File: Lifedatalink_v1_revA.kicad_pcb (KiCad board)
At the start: 4 copper layers, 76.6 x 59.8 mm, 90 parts, among them J1 DX07S024XJ1R1100, J10 503480-0400, J11 5034801400, J12 5034801400, J13 503480-0600, J14 503480-0600, J15 503480-0600, J16 503480-0600, J17 503480-0600, J18 ECG_RIGHT_LEG, J2 BATTERY CONNECTOR, J3 503480-0600, J4 Conn_01x06, J5 503480-0600, J6 ECG_LEFT_ARM, J7 ECG_RIGHT_ARM, J8 503480-0600, J9 503480-0400, P6 HORIZON MEDICAL LOGO, Q1 DMG2301L, SW1 SW_Push, U1 BL654, U2 LP5907MFX-3_3_NOPB, U3 ADS1292R, U4 MCP73831-2-OT, U5 TMP117NAIYBGR, U6 MAX30102, U7 LP5907MFX-1.8, U8 IIS2DLPCTR, U9 PCA9306, Y1 Crystal

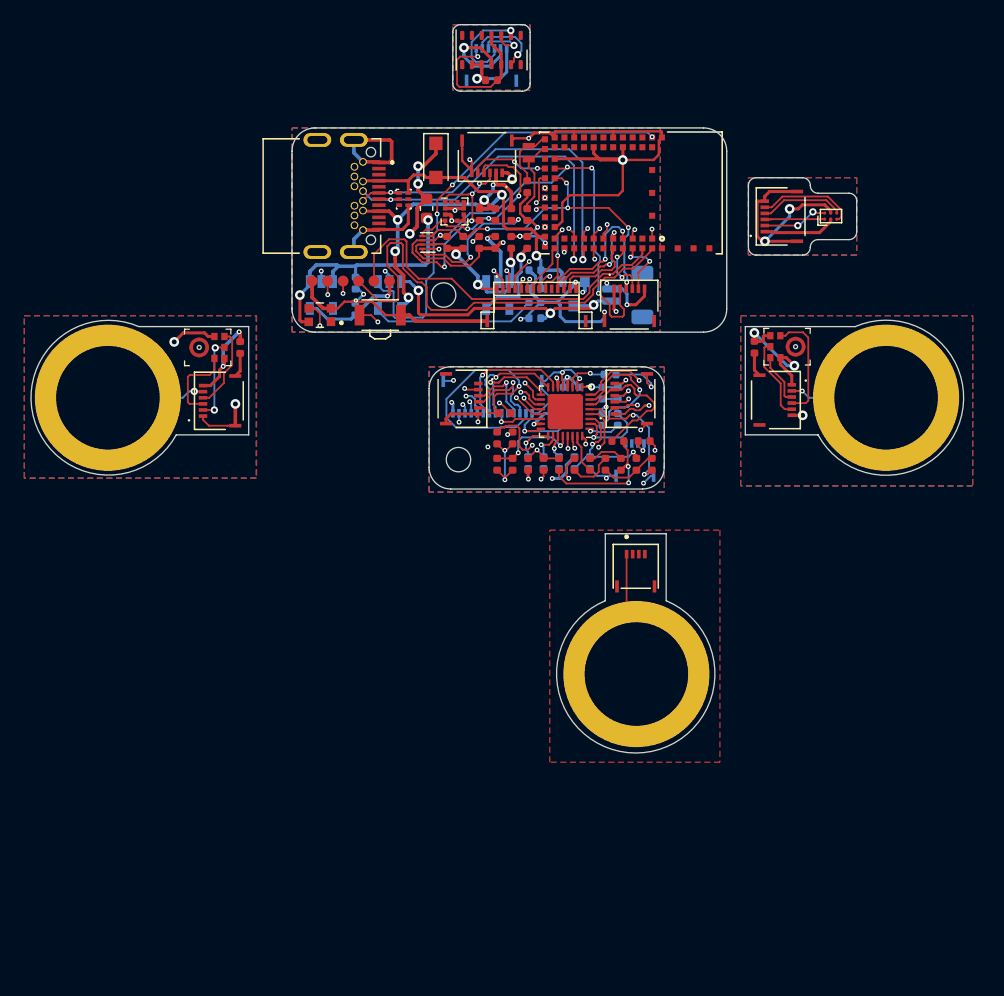
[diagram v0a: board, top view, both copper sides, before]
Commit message: Fix temperature sensor thermal pad, mounting holes, silk screen, mic ground, capacitor symmetric location and routing
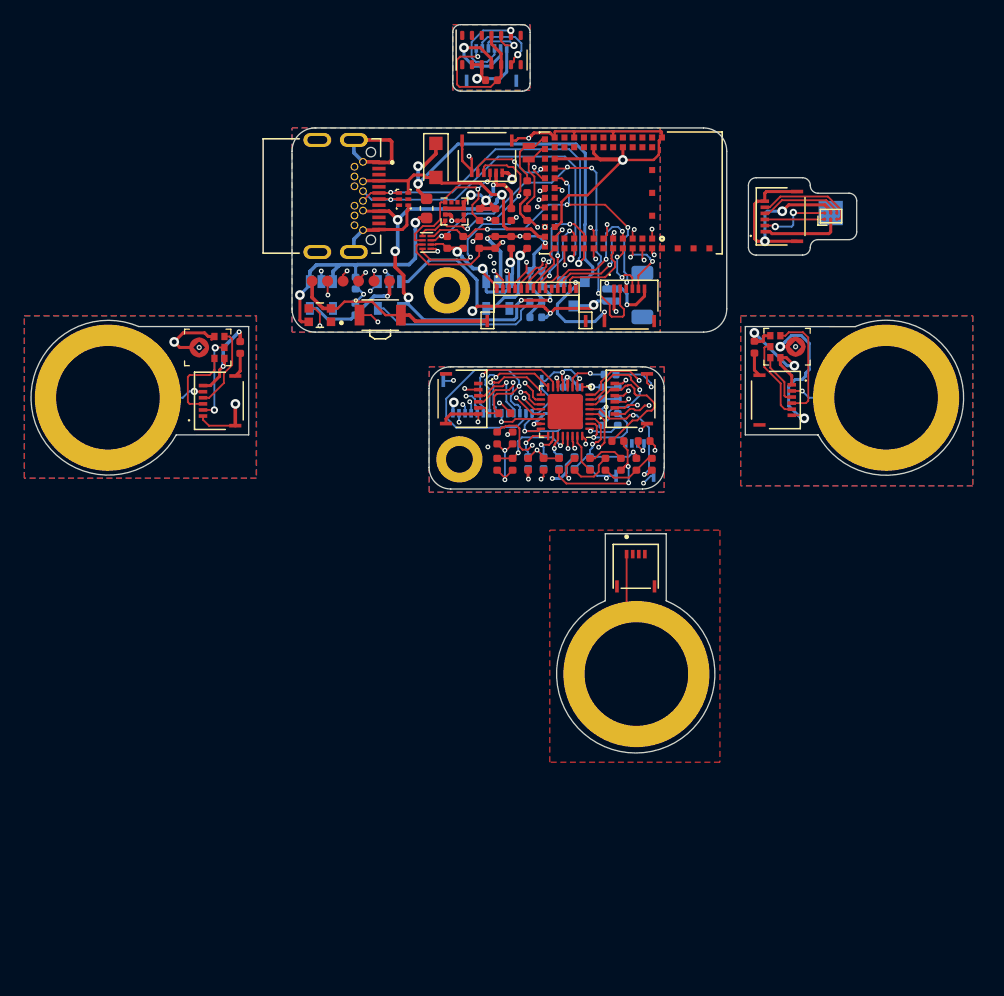
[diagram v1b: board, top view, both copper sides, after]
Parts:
- removed REF** (x2): MountingHole_2mm, MountingHole:MountingHole_2mm
- added J19: MOUNTING_HOLE_MAIN, MountingHole:MountingHole_2.2mm_M2_DIN965_Pad, F.Cu at (81.6, 107.8)
- added J20: MOUNTING_HOLE_ECG, MountingHole:MountingHole_2.2mm_M2_DIN965_Pad, F.Cu at (80.6, 93.9)
- added TPAD: TEMP_SENSOR_PAD, Pads_1.27mm:TEMP_SENSOR_PAD, B.Cu at (112.1, 87.6)
- P6: footprint horizon_logo_silk:horizon_logo_silk -> horizon_logo_silk:horizon_logo_silk_small
- moved P6 12.4 mm to (98.8, 86.7)
- moved R4 0.18 mm to (87.9, 93.6)
- moved C7 0.11 mm to (87.9, 96.1)
- moved C6 0.09 mm to (87.9, 92.3)
- moved R3 0.08 mm to (87.9, 94.9)
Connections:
- U1 pad 34: Net-(U1-Pad34) -> /MCP73831_STAT
- U1 pad 63: /MCP73831_STAT -> Net-(U1-Pad63)
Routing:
- net GND: track 242.4 -> 294.3 mm, vias 38 -> 37
- net /MCP73831_STAT: track 36.5 -> 21.9 mm, vias 3 -> 2
- net +5V: track 47.7 -> 59.0 mm, vias 5 -> 6
- net /BL654_UART_TX: track 27.5 -> 21.5 mm
- net /BL654_UART_RX: track 28.5 -> 23.0 mm
- net +3V3: track 130.8 -> 136.1 mm
- net /BL654_SWDIO: track 37.3 -> 32.3 mm, vias 0 -> 3
- net /VIN_FUSE: track 27.4 -> 32.3 mm, vias 4 -> 2
- net /BL654_I2C_SCL_LV: track 17.9 -> 13.8 mm, vias 4 -> 2
- net +BATT: track 23.0 -> 25.2 mm
- net /ADS_SPI_MOSI: track 11.8 -> 10.0 mm
- net /BL654_SWDCLK: track 30.3 -> 31.6 mm, vias 0 -> 3
- net /~ADS_SPI_CS: track 5.87 -> 7.14 mm
- net /~ADS_PWDN_RESET: track 10.5 -> 9.44 mm
- net +1V8: track 45.6 -> 44.6 mm
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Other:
- board text added: "Designed by HORIZON MEDICAL S.A.S. Cartagena - Colombia www.horizonmedical.co Model: LDL1A"
- board text removed: "LifeDataLinkv1RevA"

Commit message: Finished post routing schematic pinout and footprint cross check
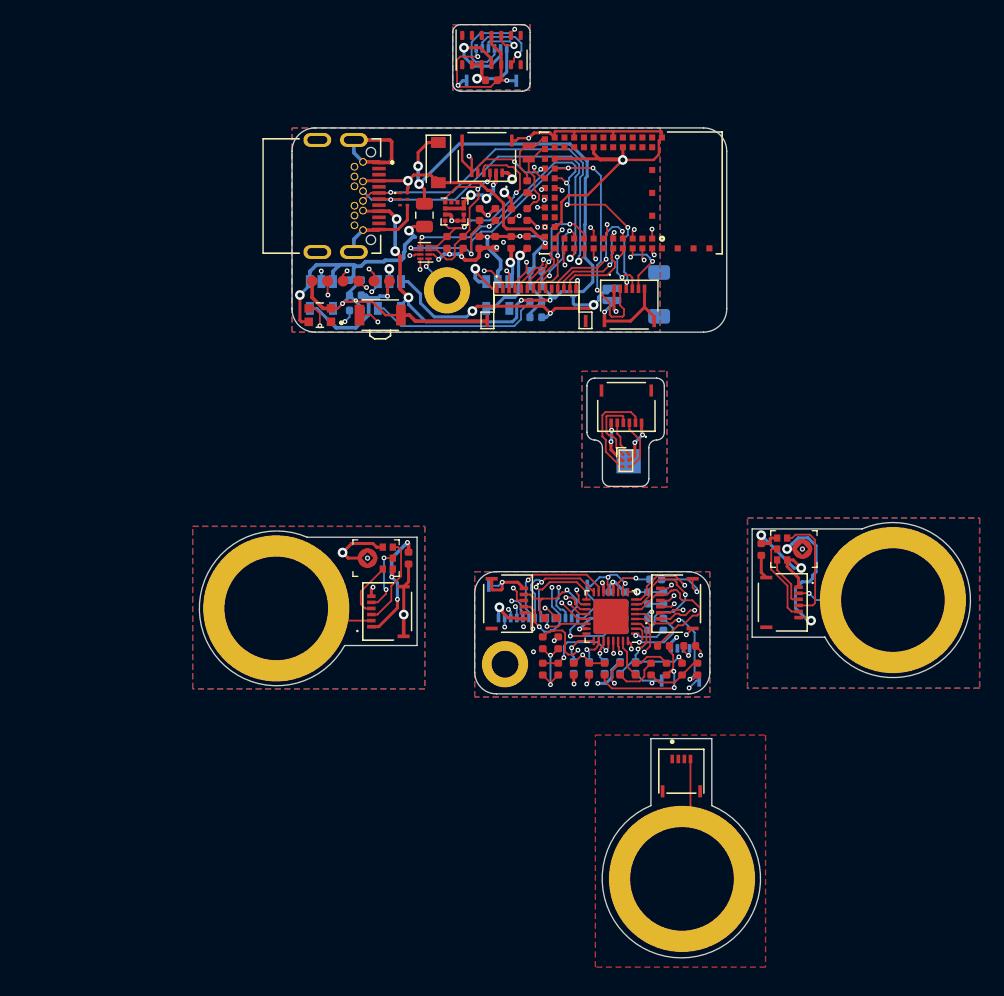
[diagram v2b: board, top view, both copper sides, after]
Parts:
- removed BAT: 401030, Battery:401030
- removed TPAD: TEMP_SENSOR_PAD, Pads_1.27mm:TEMP_SENSOR_PAD
- added C31: 100pF, Capacitor_SMD:C_0402_1005Metric, B.Cu at (73.1, 95.6)
- added REF**: TEMP_SENSOR_PAD, Pads_1.27mm:TEMP_SENSOR_PAD, B.Cu at (95.5, 108.0)
- D1: footprint digikey-footprints:UFDFN-6_1.45x1mm -> SnapEda:SON50P100X145X60-6N
- D3: footprint Diode_SMD:D_SOD-123F -> Diode_SMD:D_SOD-123
- F1: value 0603L075SLYR -> 0ZCK0075FF2E; footprint Fuse:Fuse_0603_1608Metric -> Fuse:Fuse_0805_2012Metric
- J2: value BATTERY CONNECTOR -> SM02B-SRSS-TB(LF)(SN); footprint Connector_JST:JST_SH_BM02B-SRSS-TB_1x02-1MP_P1.00mm_Vertical -> Connector_JST:JST_SH_SM02B-SRSS-TB_1x02-1MP_P1.00mm_Horizontal
- Q1: value DMG2301L -> CSD23280F3; footprint Package_TO_SOT_SMD:SOT-23 -> SnapEda:TRANS_CSD23280F3
- moved U5 26.2 mm to (95.3, 107.9), turned to 0 degrees
- moved J17 22.1 mm to (75.8, 120.3)
- moved J7 22.1 mm to (66.6, 120.0)
- moved C29 22.1 mm to (77.4, 115.9)
- moved MIC1 22.1 mm to (74.1, 115.9)
- moved J13 20.1 mm to (95.3, 103.4), turned to 180 degrees
- moved C10 17.2 mm to (98.4, 119.2)
- moved C11 17.2 mm to (97.7, 117.7)
- moved C12 17.2 mm to (93.5, 124.9)
- moved C13 17.2 mm to (98.4, 121.3)
- moved C14 17.2 mm to (97.1, 121.3)
- moved C15 17.2 mm to (93.5, 125.0)
- moved C16 17.2 mm to (98.6, 125.0)
- moved C18 17.2 mm to (97.3, 125.0)
- moved C20 17.2 mm to (99.9, 125.0)
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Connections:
- J10 pad 1: /ECG_RIGHT_LEG -> GND
- J10 pad 4: Net-(J10-Pad4) -> /ECG_RIGHT_LEG
- J13 pad 1: +3V3 -> GND
- J13 pad 2: /BL654_I2C_SCL_HV_EXT -> /TMP_ADD0_EXT
- J13 pad 3: /BL654_I2C_SDA_HV_EXT -> /TMP_ALERT_EXT
- J13 pad 4: /TMP_ALERT_EXT -> /BL654_I2C_SDA_HV_EXT
- J13 pad 5: /TMP_ADD0_EXT -> /BL654_I2C_SCL_HV_EXT
- J13 pad 6: GND -> +3V3
- J17 pad 1: GND -> +3V3
- J17 pad 2: /BL654_I2S_SD_EXT -> /ECG_RIGHT_ARM
- J17 pad 3: /BL654_I2S_SCK_EXT -> /BL654_I2S_WS_EXT
- J17 pad 4: /BL654_I2S_WS_EXT -> /BL654_I2S_SCK_EXT
- J17 pad 5: /ECG_RIGHT_ARM -> /BL654_I2S_SD_EXT
- J17 pad 6: +3V3 -> GND
- J8 pad 1: Net-(J8-Pad1) -> GND
- J8 pad 2: /ECG_RIGHT_ARM -> /BL654_I2S_SD_EXT
- J8 pad 3: /BL654_I2S_WS_EXT -> /BL654_I2S_SCK_EXT
- J8 pad 4: /BL654_I2S_SCK_EXT -> /BL654_I2S_WS_EXT
- J8 pad 5: /BL654_I2S_SD_EXT -> /ECG_RIGHT_ARM
- J8 pad 6: GND -> +3V3
- J9 pad 4: Net-(J9-Pad4) -> GND
- R17 pad 1: +1V8 -> +3V3
- R18 pad 1: +3V3 -> +1V8
- R18 pad 2: /BL654_I2C_SDA_HV -> /BL654_I2C_SDA_LV
- R19 pad 1: +3V3 -> +1V8
- R19 pad 2: /BL654_I2C_SCL_HV -> /BL654_I2C_SCL_LV
- R20 pad 1: +1V8 -> +3V3
- R20 pad 2: /BL654_I2C_SCL_LV -> /BL654_I2C_SCL_HV
- R21 pad 1: +1V8 -> +3V3
- R21 pad 2: /BL654_I2C_SDA_LV -> /BL654_I2C_SDA_HV
- U9 pad 2: +3V3 -> +1V8
- U9 pad 3: /BL654_I2C_SCL_HV -> /BL654_I2C_SCL_LV
- U9 pad 4: /BL654_I2C_SDA_HV -> /BL654_I2C_SDA_LV
- U9 pad 5: /BL654_I2C_SDA_LV -> /BL654_I2C_SDA_HV
- U9 pad 6: /BL654_I2C_SCL_LV -> /BL654_I2C_SCL_HV
- U9 pad 7: +1V8 -> +3V3
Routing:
- net GND: track 294.3 -> 275.5 mm, vias 37 -> 39
- net /BL654_I2S_SD_EXT: track 49.5 -> 33.5 mm
- net Net-(C31-Pad2): track 11.4 -> 21.1 mm, vias 2 -> 3
- net /BL654_I2C_SCL_HV: track 33.8 -> 40.3 mm, vias 4 -> 5
- net /BL654_I2C_SDA_HV: track 26.8 -> 32.8 mm, vias 5 -> 6
- net +1V8: track 44.6 -> 39.5 mm, vias 6 -> 9
- net +3V3: track 136.1 -> 140.8 mm, vias 21 -> 26
- net +5V: track 59.0 -> 54.3 mm
- net /BL654_I2C_SCL_HV_EXT: track 6.06 -> 2.99 mm, vias 2 -> 0
- net /BL654_I2S_WS_EXT: track 29.2 -> 32.1 mm, vias 2 -> 3
- net /TMP_ALERT_EXT: track 6.91 -> 4.44 mm
- net /VIN_FUSE: track 32.3 -> 34.3 mm
- net /ADS_SPI_SCLK: track 16.7 -> 18.3 mm
- net /ECG_RIGHT_ARM: track 34.6 -> 33.1 mm, vias 4 -> 3
- net +BATT: track 25.2 -> 23.8 mm
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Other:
- board size 76.6 x 59.8 mm -> 63.3 x 76.6 mm

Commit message: Added battery level voltage divider
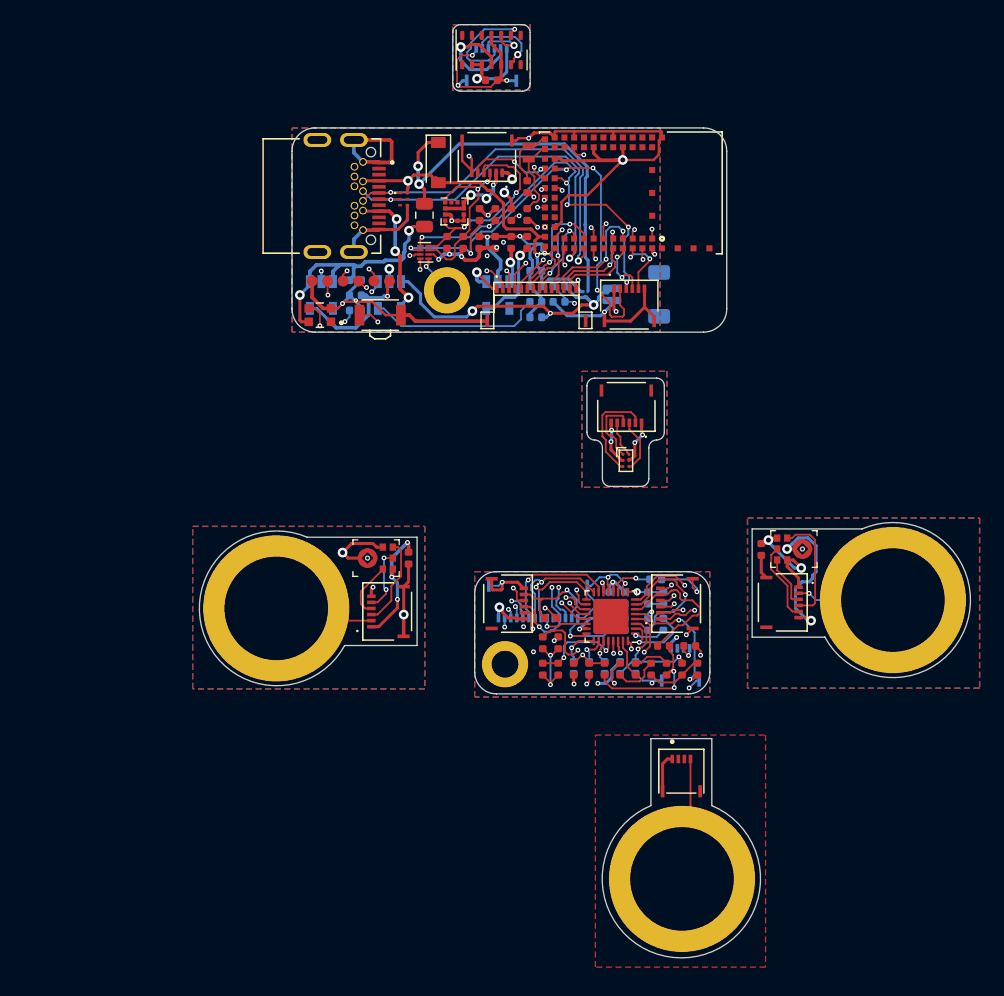
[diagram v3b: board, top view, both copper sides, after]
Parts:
- removed REF**: TEMP_SENSOR_PAD, Pads_1.27mm:TEMP_SENSOR_PAD
- added R1: 100K, Resistor_SMD:R_0402_1005Metric, B.Cu at (89.8, 93.6)
- added R2: 100K, Resistor_SMD:R_0402_1005Metric, B.Cu at (89.8, 94.9)
- moved Q1 0.99 mm to (91.9, 94.2)
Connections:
- U1 pad 48: Net-(U1-Pad48) -> /VDIV
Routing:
- net /VDIV: track 0.00 -> 20.2 mm, vias 0 -> 2
- net GND: track 275.5 -> 294.0 mm
- net +5V: track 54.3 -> 44.0 mm, vias 6 -> 5
- net +3V3: track 140.8 -> 138.6 mm
- net +BATT: track 23.8 -> 25.5 mm
- net /VIN_FUSE: track 34.3 -> 32.9 mm
- net +1V8: track 39.5 -> 40.8 mm
- net /VIN: track 20.6 -> 20.1 mm

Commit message: Changed the color of FFC connectors
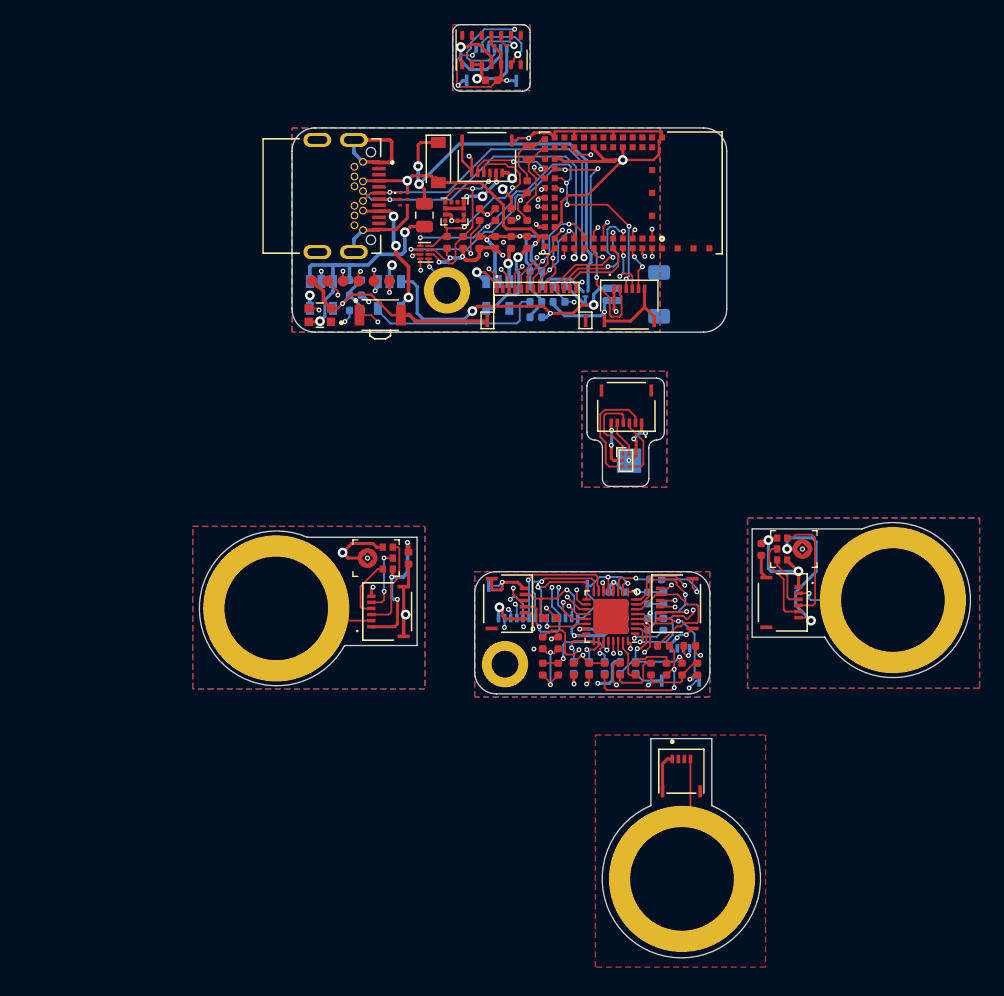
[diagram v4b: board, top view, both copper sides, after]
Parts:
- added REF**: TEMP_SENSOR_PAD, Pads_1.27mm:TEMP_SENSOR_PAD, B.Cu at (95.5, 107.9)
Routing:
- net GND: track 294.0 -> 297.9 mm
- net +3V3: track 138.6 -> 142.3 mm, vias 26 -> 28
- net /ADS_SPI_MISO: track 10.6 -> 12.4 mm
- net /TMP_ADD0: track 5.48 -> 3.79 mm
- net /BL654_SWDCLK: track 31.1 -> 29.6 mm
- net /BL654_I2S_SD_EXT: track 33.2 -> 34.4 mm
- net +BATT: track 25.5 -> 26.6 mm
- net /BL654_I2S_WS_EXT: track 32.1 -> 33.2 mm
- net /TMP_ADD0_EXT: track 8.51 -> 9.50 mm
- net +1V8: track 40.8 -> 39.8 mm
- net /~ADS_SPI_CS_EXT: track 10.3 -> 11.2 mm
- net /VIN: track 20.1 -> 21.0 mm
- net /BL654_SWDIO: track 32.4 -> 31.5 mm
- net Net-(C18-Pad1): track 3.70 -> 4.49 mm
- net /WS2812_DATA: track 38.8 -> 38.0 mm
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
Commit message: Fixed electrode boards
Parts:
- moved J7 2.36 mm to (67.9, 118.1)
- moved C29 1.94 mm to (79.3, 115.5)
- moved J17 1.94 mm to (77.7, 119.9)
- moved MIC1 1.94 mm to (76.0, 115.5)
- moved J6 1.29 mm to (116.8, 118.1)
- moved J10 1.02 mm to (99.7, 132.7), turned to 180 degrees
- moved J5 0.97 mm to (107.2, 119.9)
- moved MIC2 0.97 mm to (108.9, 115.5)
- moved C30 0.97 mm to (105.5, 115.6)
- moved J13 0.64 mm to (95.3, 102.8)
- moved U5 0.63 mm to (95.3, 107.3)
- moved REF** 0.35 mm to (95.2, 107.7)
- moved J18 0.19 mm to (99.7, 142.2)
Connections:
- J10 pad 1: GND -> /ECG_RIGHT_LEG
- J10 pad 4: /ECG_RIGHT_LEG -> GND
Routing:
- net GND: track 297.9 -> 301.9 mm, vias 39 -> 38
- net +3V3: track 142.3 -> 144.4 mm
- net /ECG_RIGHT_LEG: track 11.8 -> 10.2 mm
- net /ECG_RIGHT_ARM: track 33.4 -> 34.6 mm
- net /BL654_I2S_WS_EXT: track 33.2 -> 32.6 mm
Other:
- board size 63.3 x 76.6 mm -> 62.4 x 77 mm

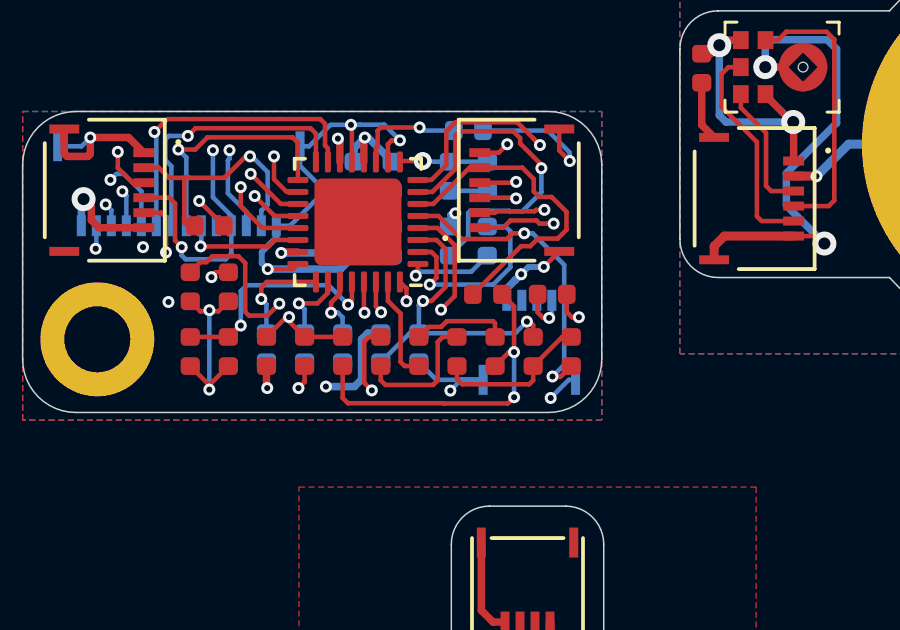
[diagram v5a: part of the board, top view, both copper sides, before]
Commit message: Fixed small routing traces
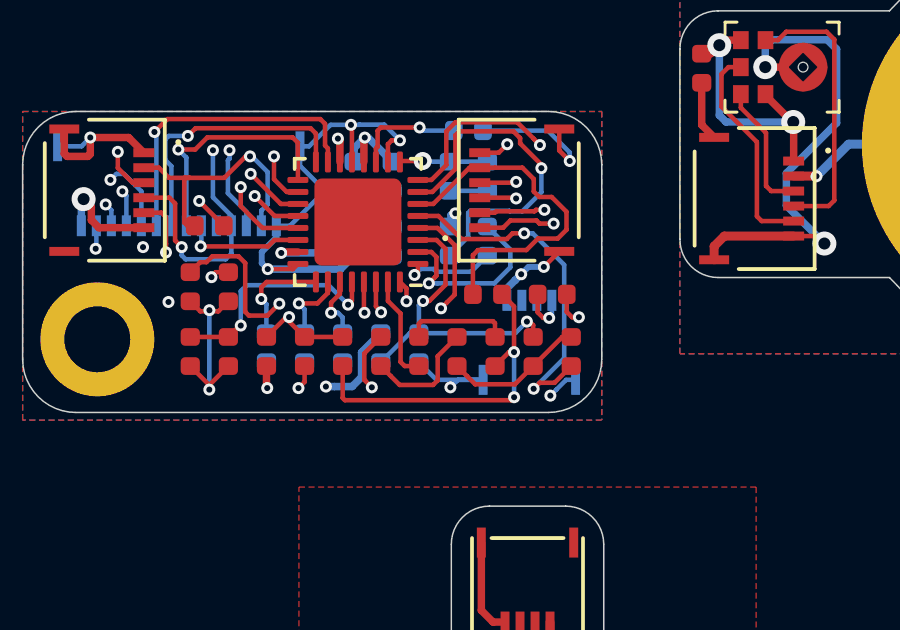
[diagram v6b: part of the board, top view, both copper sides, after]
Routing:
- net /ECG_RIGHT_ARM: track 34.6 -> 36.0 mm
- net /ECG_LEFT_ARM: track 19.6 -> 20.4 mm
- net Net-(C18-Pad1): track 4.49 -> 3.93 mm
- net Net-(C18-Pad2): track 5.25 -> 4.71 mm

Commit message: Finalized and exported CAD files for quotation
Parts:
- C29, C30: value 0.1uF -> 100nF
- U3: value ADS1292R -> ADS1292RIRSMT
- U4: value MCP73831-2-OT -> MCP73831T-2ACI/OT
- U7: value LP5907MFX-1.8 -> LP5907MFX-1.8/NOPB
- U9: value PCA9306 -> PCA9306DQER
- moved C10 4.57 mm to (98.2, 114.6)
- moved C12 4.57 mm to (93.4, 120.3)
- moved C13 4.57 mm to (98.2, 116.8)
- moved C14 4.57 mm to (97.0, 116.8)
- moved C22 4.57 mm to (95.1, 116.8)
- moved C23 4.57 mm to (93.8, 116.8)
- moved C29 4.57 mm to (79.2, 111.0)
- moved C30 4.57 mm to (105.4, 111.0)
- moved C5 4.57 mm to (93.8, 114.6)
- moved C8 4.57 mm to (95.1, 114.6)
- moved C9 4.57 mm to (97.0, 114.6)
- moved J10 4.57 mm to (99.6, 128.1)
- moved J11 4.57 mm to (87.9, 116.3)
- moved J17 4.57 mm to (77.6, 115.3)
- moved J18 4.57 mm to (99.6, 137.7)
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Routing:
- net GND: track 301.6 -> 308.2 mm, vias 38 -> 42
- net /BL654_I2S_SD_EXT: track 34.4 -> 35.5 mm
- net Net-(C21-Pad2): track 20.4 -> 21.5 mm
- net Net-(C20-Pad2): track 10.4 -> 11.2 mm
- net /ECG_LEFT_ARM: track 20.4 -> 19.8 mm
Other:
- board size 62.4 x 77 mm -> 62.4 x 72.4 mm
- board text added: "Designed by HORIZON MEDICAL S.A.S. Cartagena - Colombia www.horizonmedical.co Model: HZLDL1A"
- board text removed: "Designed by HORIZON MEDICAL S.A.S. Cartagena - Colombia www.horizonmedical.co Model: LDL1A"
